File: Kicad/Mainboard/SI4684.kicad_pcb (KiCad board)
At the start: 2 copper layers, 41.6 x 42.2 mm, 88 parts, among them J1 Conn_01x03, J3 Headphones, J5 DISP LEFT, J6 DISP RIGHT, J7 Conn_01x02_Pin, J8 Conn_01x02_Pin, Q2 2N7002, SW4 SW_Push, SW5 SW_Push, SW6 SW_Push, U1 MIC5504-1.8YM5, U12 SIQ-02FVS3, U2 BME680, U3 SI4684-A10-GM, U4 TCA9554PW, U5 TPA6130A2RTJTG4, U6 RT9013, X1 19.2MHz

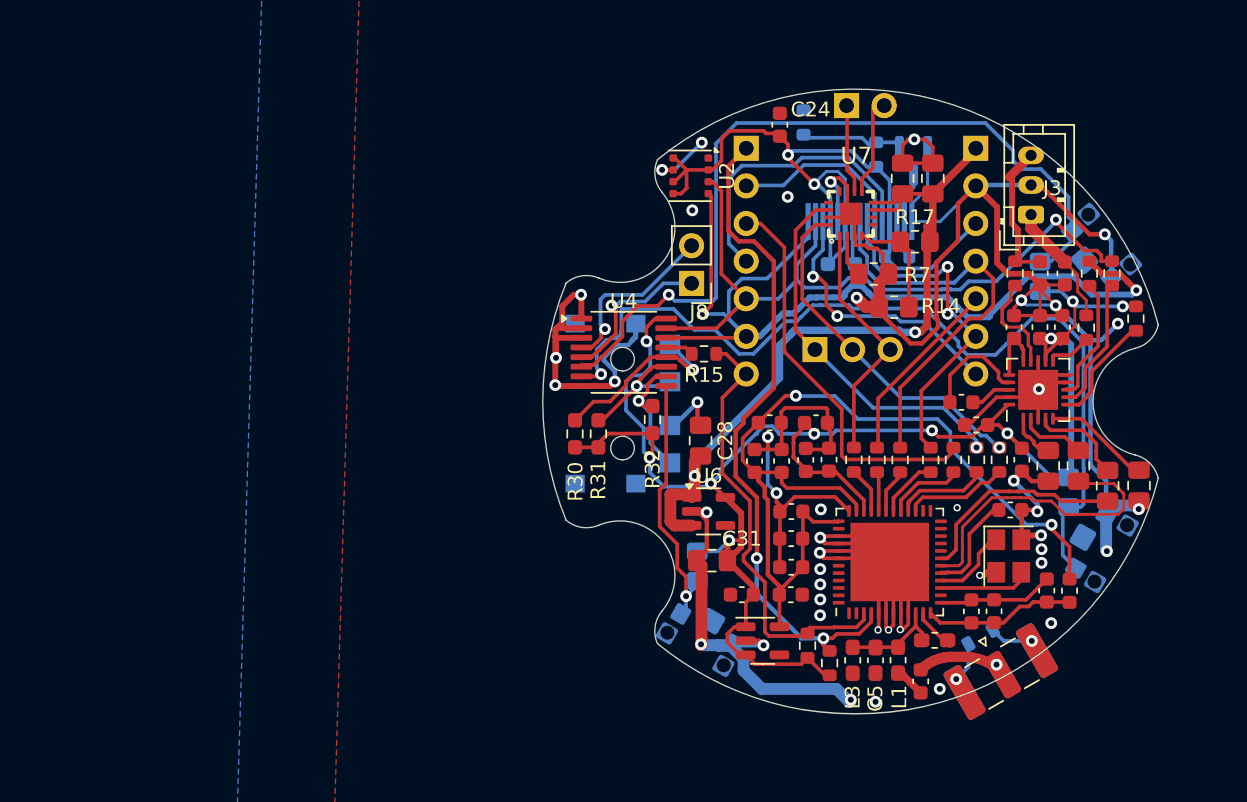
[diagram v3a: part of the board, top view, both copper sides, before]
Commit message: Add files via upload
- Added second Rotary encoder
- Removed need for Motherboard
- Removed Switch P4 (Slideshow Switch)
- Did a lot of Rerouting
- Performed some DRC Checks
(still not final)... work in Progress
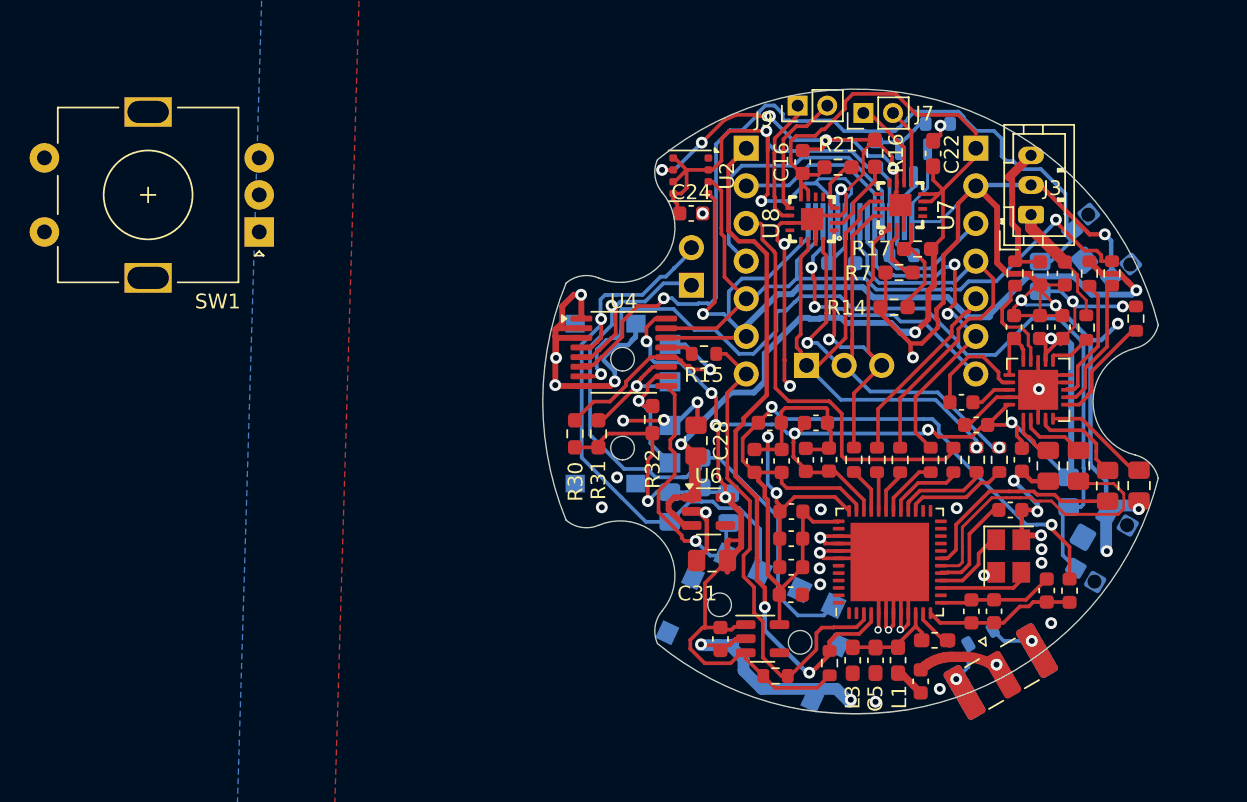
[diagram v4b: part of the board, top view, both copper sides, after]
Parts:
- removed SW4: SW_Push, tp4056:SW_SPST_CK_KMS2xxGP
- added J9: Conn_01x02_Pin, Connector_PinHeader_2.00mm:PinHeader_1x02_P2.00mm_Vertical, F.Cu at (95.6, 80.2)
- added R16: 100K, Resistor_SMD:R_0603_1608Metric_Pad0.98x0.95mm_HandSolder, F.Cu at (100.8, 83.4)
- added R21: 330K, Resistor_SMD:R_0603_1608Metric_Pad0.98x0.95mm_HandSolder, F.Cu at (98.3, 84.3)
- added R35: 10k, Resistor_SMD:R_0805_2012Metric_Pad1.20x1.40mm_HandSolder, B.Cu at (87.0, 107.3)
- added R36: 10k, Resistor_SMD:R_0805_2012Metric_Pad1.20x1.40mm_HandSolder, B.Cu at (89.0, 105.0)
- added SW1: RotaryEncoder_Switch, Rotary_Encoder:RotaryEncoder_Alps_EC11E-Switch_Vertical_H20mm, F.Cu at (59.3, 88.7)
- added U14: SIQ-02FVS3, tp4056:SW-SMD_SIQ-02FVS3_1, B.Cu at (92.2, 117.0)
- added U8: ~, tp4056:TQFN-16_L3.0-W3.0-P0.50-BL-EP1.5, F.Cu at (96.6, 87.8)
- C16: footprint Capacitor_SMD:C_0805_2012Metric_Pad1.18x1.45mm_HandSolder -> Capacitor_SMD:C_0603_1608Metric
- C22: footprint Capacitor_SMD:C_0805_2012Metric_Pad1.18x1.45mm_HandSolder -> Capacitor_SMD:C_0603_1608Metric_Pad1.08x0.95mm_HandSolder
- J7: footprint Connector_PinHeader_2.54mm:PinHeader_1x02_P2.54mm_Vertical -> Connector_PinHeader_2.00mm:PinHeader_1x02_P2.00mm_Vertical; moved to F.Cu
- J8: moved to B.Cu
- R14, R17, R7: footprint Resistor_SMD:R_0805_2012Metric_Pad1.20x1.40mm_HandSolder -> Resistor_SMD:R_0603_1608Metric_Pad0.98x0.95mm_HandSolder
- moved R19 9.07 mm to (105.1, 81.4), turned to 180 degrees
- moved C16 8.86 mm to (96.0, 84.0)
- moved C24 8.46 mm to (88.4, 87.5), turned to 0 degrees
- moved R27 4.46 mm to (91.0, 107.3)
- moved U7 3.40 mm to (102.6, 86.9)
- moved C1 3.32 mm to (90.4, 116.2), turned to -90 degrees
- moved R26 2.98 mm to (94.1, 118.7), turned to 0 degrees
- moved C22 2.66 mm to (104.8, 83.4)
- moved R7 1.72 mm to (102.5, 91.4), turned to 0 degrees
- moved J7 1.24 mm to (100.1, 80.7), turned to 90 degrees
- moved J1 1.21 mm to (96.2, 97.7)
- moved R17 0.52 mm to (103.7, 89.8)
- moved R22 0.33 mm to (102.7, 90.3)
- moved C28 0.31 mm to (88.8, 102.8)
- moved Q2 0.16 mm to (103.4, 84.0)
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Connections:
- U12 pad 5: unconnected-(U12-EH-Pad5) -> GND
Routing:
- net GND: track 239.3 -> 277.2 mm, vias 45 -> 50
- net P1: track 11.0 -> 47.0 mm
- net P0: track 12.1 -> 40.2 mm
- net +5V: track 51.9 -> 72.7 mm
- net I2SLRC: track 25.3 -> 37.2 mm
- net I2SDIN: track 16.7 -> 28.4 mm, vias 0 -> 1
- net I2SCLK: track 23.7 -> 35.2 mm, vias 1 -> 2
- net +3.3VA: track 53.3 -> 63.5 mm
- net Net-(J9-Pin_1): track 0.00 -> 8.80 mm
- net Net-(J9-Pin_2): track 0.00 -> 8.73 mm
- net +3V3: track 121.3 -> 128.9 mm, vias 10 -> 11
- net Net-(U8-GAIN): track 0.00 -> 5.26 mm
- net Net-(U8-SD): track 0.00 -> 4.05 mm
- net INT: track 30.1 -> 33.6 mm
- net P2: track 54.4 -> 57.3 mm
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
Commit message: Add files via upload
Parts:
- removed SW1: RotaryEncoder_Switch, Rotary_Encoder:RotaryEncoder_Alps_EC11E-Switch_Vertical_H20mm
- added R33: 0R, Resistor_SMD:R_0603_1608Metric, F.Cu at (91.0, 111.3)
- added R37: 0R, Resistor_SMD:R_0603_1608Metric, F.Cu at (92.6, 111.5)
- moved R34 4.96 mm to (98.3, 85.9)
- moved U13 3.55 mm to (99.5, 91.3)
- moved R22 3.28 mm to (103.0, 87.0)
- moved C31 1.85 mm to (88.4, 112.0), turned to -90 degrees
- moved R21 0.78 mm to (98.3, 83.5)
- moved J1 0.51 mm to (96.2, 98.2)
- moved R19 0.28 mm to (104.8, 81.4)
- moved C16 0.10 mm to (95.9, 84.0)
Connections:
- R25 pad 2: RST -> Net-(U3-RSTB)
- R26 pad 2: INT -> Net-(U3-INTB)
- U3 pad 3: INT -> Net-(U3-INTB)
- U3 pad 4: RST -> Net-(U3-RSTB)
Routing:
- net INT: track 33.6 -> 16.4 mm
- net RST: track 47.8 -> 31.4 mm, vias 2 -> 0
- net Net-(U3-INTB): track 0.00 -> 15.6 mm
- net Net-(U3-RSTB): track 0.00 -> 15.0 mm, vias 0 -> 2
- net GND: track 277.2 -> 290.2 mm, vias 50 -> 55
- net +3.3VA: track 63.5 -> 68.3 mm
- net /LEDK: track 3.43 -> 7.67 mm
- net CLK: track 25.1 -> 29.3 mm
- net TP2_INT: track 19.1 -> 23.2 mm
- net LCD_DC: track 20.6 -> 23.9 mm
- net LCD_CS: track 12.0 -> 15.3 mm
- net Net-(U13-RST): track 2.89 -> 5.55 mm
- net Net-(U13-LEDA): track 2.70 -> 5.20 mm
- net SCL: track 64.2 -> 61.8 mm
- net P3: track 62.4 -> 60.9 mm
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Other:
- board text added: "1"
- board text added: "connector zeigt hier. TOP Contacts"

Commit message: Add files via upload
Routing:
- net GND: track 290.2 -> 305.9 mm
- net +3V3: track 128.4 -> 125.7 mm
- net Net-(ANT1-A): track 7.52 -> 5.92 mm
- net P3: track 60.9 -> 59.3 mm
- net SCL: track 61.8 -> 60.7 mm
- net +5V: track 73.5 -> 72.4 mm
- net Net-(Q2-G): track 4.60 -> 3.63 mm
- net I2SCLK: track 35.0 -> 34.2 mm
- net P1: track 46.7 -> 46.0 mm
- net Net-(U3-RSTB): track 15.0 -> 14.3 mm
- net P6: track 8.52 -> 7.88 mm
- net +1V8: track 61.3 -> 60.7 mm
- net LCD_DC: track 23.9 -> 23.3 mm
- net Net-(J3-Pin_3): track 9.63 -> 9.07 mm
- net MOSI: track 28.9 -> 28.3 mm
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
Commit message: Add files via upload
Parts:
- added D2: LED, LED_SMD:LED_1210_3225Metric_Pad1.42x2.65mm_HandSolder, B.Cu at (94.4, 107.5)
- added D3: LED, LED_SMD:LED_1210_3225Metric, B.Cu at (110.8, 91.8)
- added D4: LED, LED_SMD:LED_1210_3225Metric_Pad1.42x2.65mm_HandSolder, B.Cu at (116.2, 105.1)
- added D5: LED, LED_SMD:LED_1210_3225Metric_Pad1.42x2.65mm_HandSolder, B.Cu at (94.1, 103.5)
- added H2: MountingHole, baer_klein:baerklein, B.Cu at (103.1, 112.2)
- added J2: Conn_01x05, Connector_PinSocket_2.54mm:PinSocket_1x05_P2.54mm_Vertical_SMD_Pin1Left, B.Cu at (103.8, 109.1)
- added Q1: 2N7002, Package_TO_SOT_SMD:SOT-23, F.Cu at (81.5, 106.2)
- added R20: 100, Resistor_SMD:R_0603_1608Metric, F.Cu at (84.1, 106.4)
- added TP1: TestPoint, TestPoint:TestPoint_Pad_D1.0mm, F.Cu at (85.8, 104.3)
- C10, C9: value 1uF -> 10uF
- C16: value 10uF -> 1uF
- R1: value 4k7 -> 10k
- R10, R11: value 220 -> 100
- U2: value BME680 -> BME688
- U5: value TPA6130A2RTJTG4 -> TPA6130A2RTJTR
- U7, U8: value ~ -> MAX98357AETE
- X1: value 19.2MHz -> S3219200071060
- moved R29 5.45 mm to (113.8, 100.8)
- moved R36 2.55 mm to (90.5, 102.8), turned to -90 degrees
- moved ANT 1.80 mm to (110.9, 117.6), turned to -55 degrees
- moved D1 1.72 mm to (109.8, 115.8), turned to -55 degrees
- moved R28 1.45 mm to (113.4, 92.0)
- moved C3 1.43 mm to (104.7, 117.8), turned to 180 degrees
- moved L2 0.89 mm to (114.1, 112.0)
- moved C6 0.86 mm to (112.5, 112.0)
- moved R8 0.53 mm to (116.4, 91.3)
- moved C39 0.53 mm to (111.8, 92.0)
- moved R11 0.50 mm to (110.3, 92.0)
- moved C34 0.50 mm to (113.4, 91.9)
- moved J3 0.49 mm to (111.3, 88.0)
- moved R9 0.48 mm to (114.9, 91.3)
- moved R4 0.41 mm to (104.2, 104.1)
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- renumbered ANT1 to ANT
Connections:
- net Net-(ANT1-A) renamed ANT
- SW6 pad 1: GND -> P3
- SW6 pad 2: P3 -> GND
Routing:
- net GND: track 305.9 -> 375.6 mm, vias 55 -> 54
- net MOSI: track 28.3 -> 35.8 mm, vias 0 -> 1
- net Net-(Q1-D): track 0.00 -> 7.09 mm
- net CLK: track 28.9 -> 35.5 mm, vias 2 -> 3
- net SS: track 29.1 -> 34.7 mm, vias 0 -> 1
- net MISO: track 12.4 -> 17.3 mm, vias 0 -> 1
- net P2: track 57.2 -> 61.6 mm
- net I2SLRC: track 37.4 -> 39.5 mm
- net Net-(U3-DBYP): track 27.3 -> 29.3 mm
- net P0: track 39.7 -> 41.6 mm, vias 1 -> 2
- net P3: track 59.3 -> 57.4 mm
- net ANT: track 5.92 -> 7.53 mm
- net Net-(Q1-G): track 0.00 -> 1.48 mm
- net I2SDIN: track 29.1 -> 30.4 mm
- net Net-(U3-ABYP): track 7.63 -> 8.78 mm
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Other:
- board text added: "3V"
- board text added: "5V"
- board text added: "Double Check U3 & U5 Orientation! connector zeigt hier. TOP Contacts"
- board text added: "GD"
- board text added: "SCL"
- board text added: "SDA"
- board text added: "SPIZIG @2025"
- board text removed: "connector zeigt hier. TOP Contacts"
